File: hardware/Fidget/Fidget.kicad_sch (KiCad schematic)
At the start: 38 parts

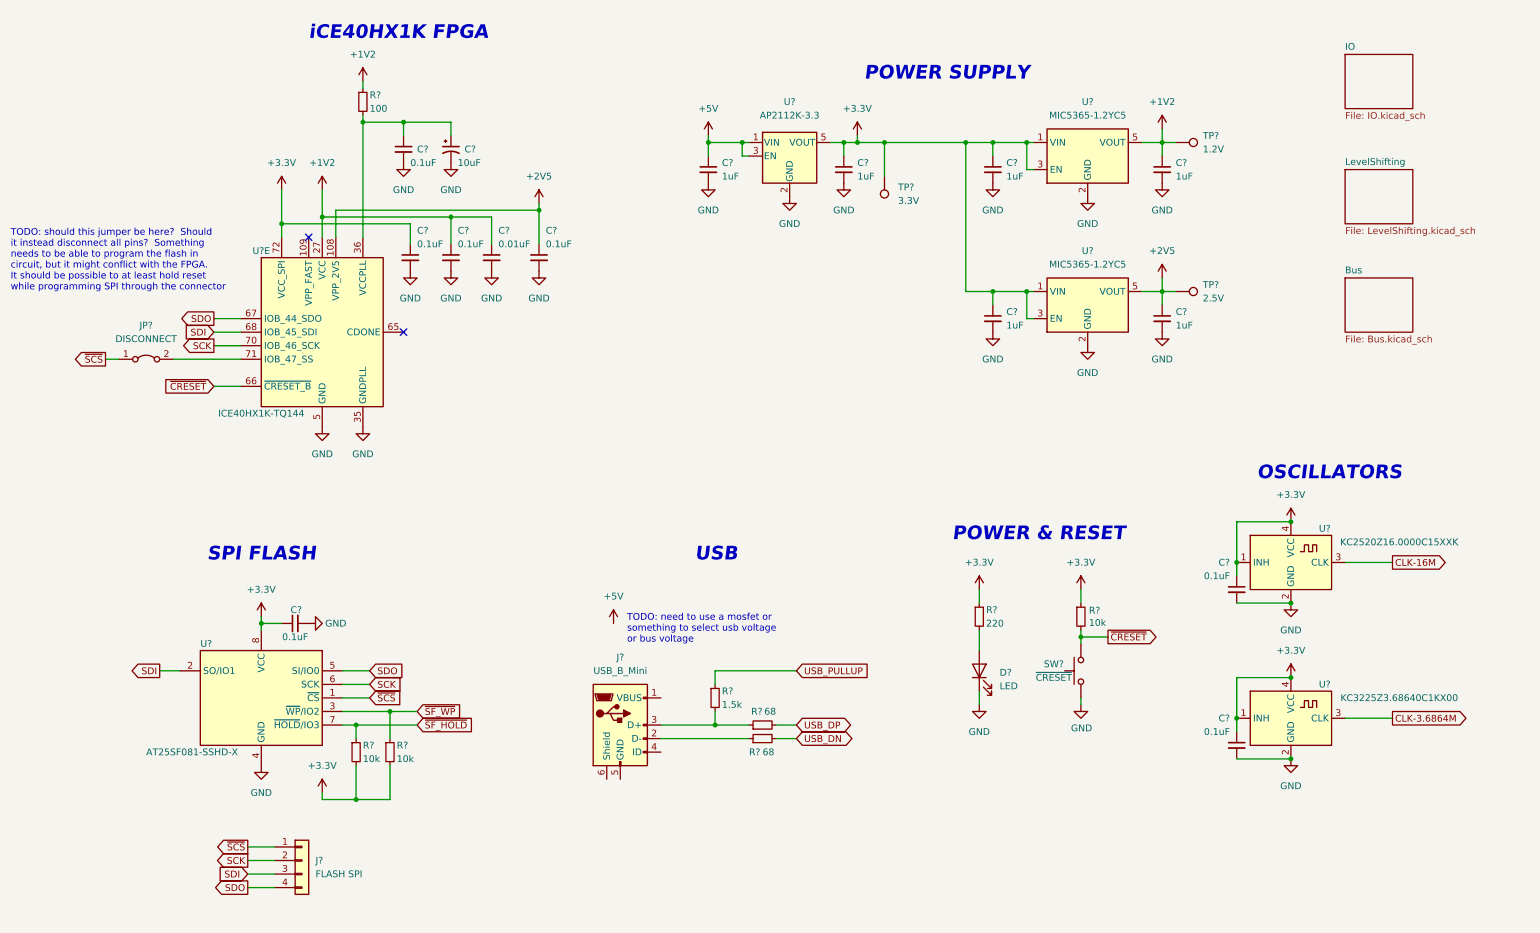
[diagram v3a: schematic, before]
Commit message: Added address latches
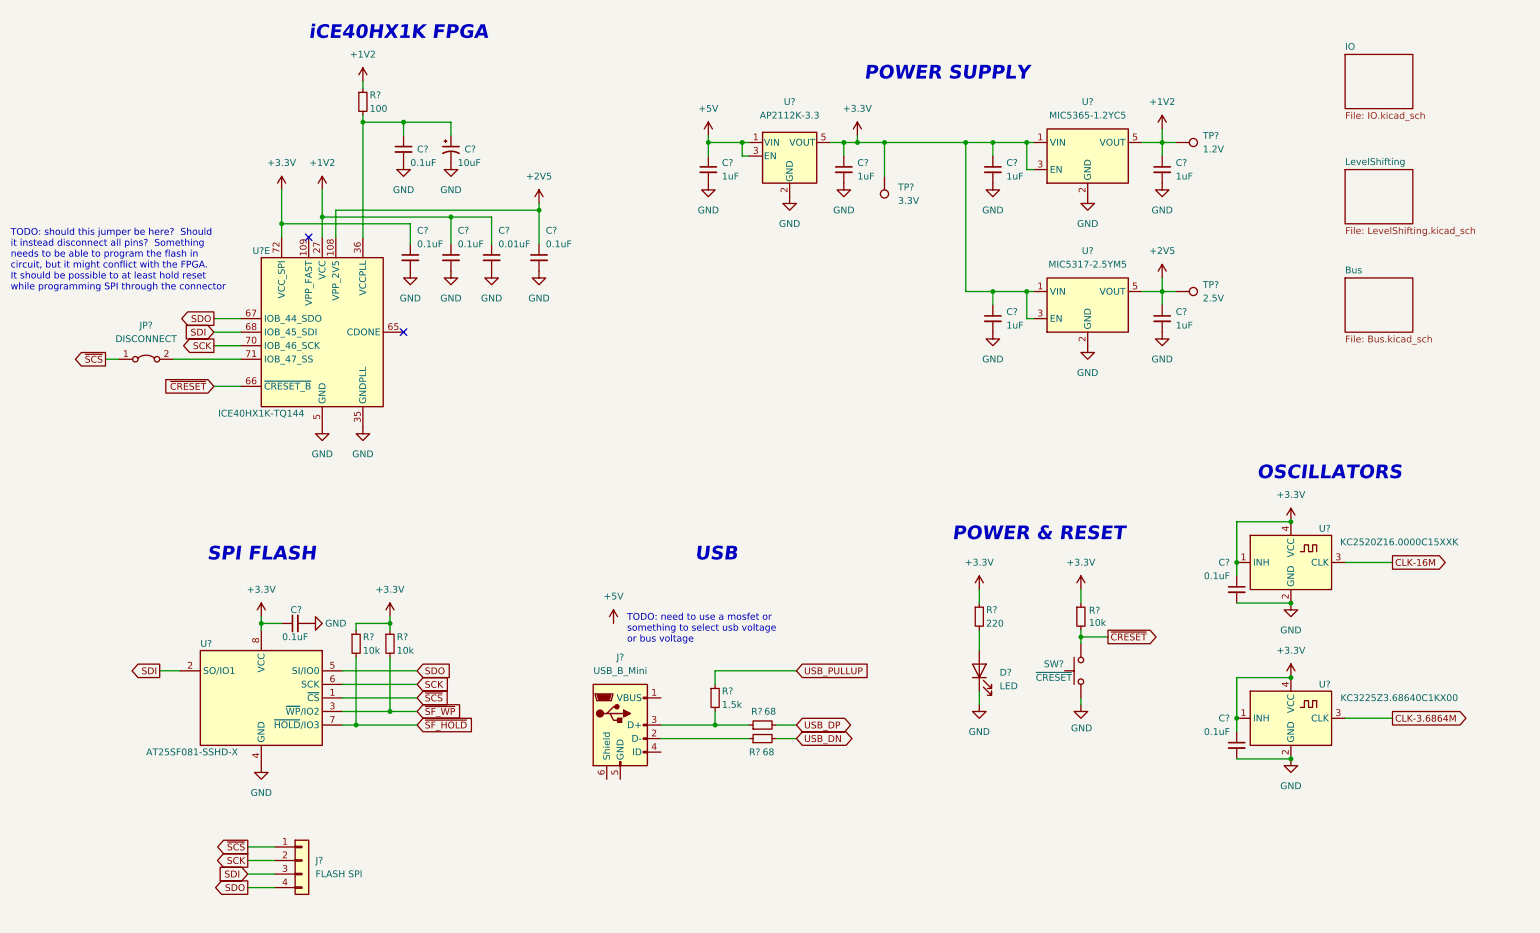
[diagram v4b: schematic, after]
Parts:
- U?: value MIC5365-1.2YC5 -> MIC5317-2.5YM5; footprint Package_TO_SOT_SMD:SOT-353_SC-70-5 -> Package_TO_SOT_SMD:SOT-23-5_HandSoldering
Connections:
- net +3.3V: now also R?.1, R?.1; no longer R?.2, R?.2
- net ~{SF_HOLD}: now also R?.2; no longer R?.1
- net ~{SF_WP}: now also R?.2; no longer R?.1
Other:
- moved on the sheet: R?

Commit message: Added jumper to select bus voltage
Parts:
- added JP?: VBUS, symbol Jumper:Jumper_3_Bridged12
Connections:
- net +3.3V: now also JP?.3 (B)
- net +5V: now also JP?.1 (A)
- new net VBUS: JP?.2 (C)
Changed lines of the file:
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@@
+    (stroke (width 0) (type default) (color 0 0 0 0))
+  )
+  (wire (pts (xy 157.48 71.12) (xy 161.29 71.12))
     (stroke (width 0) (type default) (color 0 0 0 0))
   )
@@
     (stroke (width 0) (type default) (color 0 0 0 0))
   )
+  (wire (pts (xy 140.97 71.12) (xy 144.78 71.12))
+    (stroke (width 0) (type default) (color 0 0 0 0))
+  )
   (wire (pts (xy 196.85 44.45) (xy 195.58 44.45))
     (stroke (width 0) (type default) (color 0 0 0 0))
@@
     (stroke (width 0) (type default) (color 0 0 0 0))
   )
+  (wire (pts (xy 157.48 81.28) (xy 151.13 81.28))
+    (stroke (width 0) (type default) (color 0 0 0 0))
+  )
   (wire (pts (xy 78.74 35.56) (xy 87.63 35.56))
     (stroke (width 0) (type default) (color 0 0 0 0))
@@
     (stroke (width 0) (type default) (color 0 0 0 0))
   )
+  (wire (pts (xy 151.13 81.28) (xy 151.13 74.93))
+    (stroke (width 0) (type default) (color 0 0 0 0))
+  )
   (wire (pts (xy 104.14 52.07) (xy 104.14 58.42))
     (stroke (width 0) (type default) (color 0 0 0 0))
@@
   )
   (wire (pts (xy 55.88 54.61) (xy 80.01 54.61))
+    (stroke (width 0) (type default) (color 0 0 0 0))
+  )
+  (wire (pts (xy 140.97 69.85) (xy 140.97 71.12))
     (stroke (width 0) (type default) (color 0 0 0 0))
   )
@@
     (pin "1")
   )
+  (symbol (lib_id "power:+5V") (at 140.97 69.85 0) (unit 1)
+    (in_bom yes) (on_board yes) (fields_autoplaced)
+    (property "Reference" "#PWR?" (id 0) (at 140.97 73.66 0)
+      (effects (font (size 1.27 1.27)) hide)
+    )
+    (property "Value" "+5V" (id 1) (at 140.97 64.77 0))
+    (property "Footprint" "" (id 2) (at 140.97 69.85 0)
+      (effects (font (size 1.27 1.27)) hide)
+    )
+    (property "Datasheet" "" (id 3) (at 140.97 69.85 0)
+      (effects (font (size 1.27 1.27)) hide)
+    )
+    (pin "1")
+  )
   (symbol (lib_id "power:+3.3V") (at 205.74 123.19 0) (unit 1)
     (in_bom yes) (on_board yes) (fields_autoplaced)
@@
     (pin "8")
   )
+  (symbol (lib_id "power:+3.3V") (at 161.29 71.12 0) (unit 1)
+    (in_bom yes) (on_board yes) (fields_autoplaced)
+    (property "Reference" "#PWR?" (id 0) (at 161.29 74.93 0)
+      (effects (font (size 1.27 1.27)) hide)
+    )
+    (property "Value" "+3.3V" (id 1) (at 161.29 66.04 0))
+    (property "Footprint" "" (id 2) (at 161.29 71.12 0)
+      (effects (font (size 1.27 1.27)) hide)
+    )
+    (property "Datasheet" "" (id 3) (at 161.29 71.12 0)
+      (effects (font (size 1.27 1.27)) hide)
+    )
+    (pin "1")
+  )
+  (symbol (lib_id "power:VBUS") (at 157.48 81.28 0) (unit 1)
+    (in_bom yes) (on_board yes) (fields_autoplaced)
+    (property "Reference" "#PWR?" (id 0) (at 157.48 85.09 0)
+      (effects (font (size 1.27 1.27)) hide)
+    )
+    (property "Value" "VBUS" (id 1) (at 157.48 76.2 0))
+    (property "Footprint" "" (id 2) (at 157.48 81.28 0)
+      (effects (font (size 1.27 1.27)) hide)
+    )
+    (property "Datasheet" "" (id 3) (at 157.48 81.28 0)
+      (effects (font (size 1.27 1.27)) hide)
+    )
+    (pin "1")
+  )
   (symbol (lib_id "Device:R_Small") (at 146.05 148.59 90) (unit 1)
     (in_bom yes) (on_board yes)
@@
     )
     (pin "1")
+  )
+  (symbol (lib_id "Jumper:Jumper_3_Bridged12") (at 151.13 71.12 0) (unit 1)
+    (in_bom yes) (on_board yes) (fields_autoplaced)
+    (property "Reference" "JP?" (id 0) (at 151.13 64.77 0))
+    (property "Value" "VBUS" (id 1) (at 151.13 67.31 0))
+    (property "Footprint" "" (id 2) (at 151.13 71.12 0)
+      (effects (font (size 1.27 1.27)) hide)
+    )
+    (property "Datasheet" "~" (id 3) (at 151.13 71.12 0)
+      (effects (font (size 1.27 1.27)) hide)
+    )
+    (pin "1")
+    (pin "2")
+    (pin "3")
   )
   (symbol (lib_id "power:GND") (at 207.01 77.47 0) (unit 1)
@@
       (reference "#PWR0135") (unit 1) (value "+3.3V") (footprint "")
     )
-    (path "/636ee855-2082-46e2-a822-b2da99283a14/6fc735af-e2e1-4ebe-9b58-edde6986a065"
-      (reference "#PWR0136") (unit 1) (value "+5V") (footprint "")
-    )
     (path "/636ee855-2082-46e2-a822-b2da99283a14/ce525dd6-668d-4227-a847-a3e1bacd0f50"
       (reference "#PWR0137") (unit 1) (value "GND") (footprint "")
@@
       (reference "#PWR?") (unit 1) (value "GND") (footprint "")
     )
+    (path "/636ee855-2082-46e2-a822-b2da99283a14/0c5bded0-c97a-4fbd-beaf-a61fa33b10ae"
+      (reference "#PWR?") (unit 1) (value "VBUS") (footprint "")
+    )
+    (path "/636ee855-2082-46e2-a822-b2da99283a14/0cf0cba3-5d9e-44c7-a28f-17652c4b4436"
+      (reference "#PWR?") (unit 1) (value "VBUS") (footprint "")
+    )
+    (path "/636ee855-2082-46e2-a822-b2da99283a14/10b1bab0-c952-444c-8358-2913aeb4fe24"
+      (reference "#PWR?") (unit 1) (value "VBUS") (footprint "")
+    )
     (path "/636ee855-2082-46e2-a822-b2da99283a14/11563f15-8da5-437f-b4e1-2d5ae629ea03"
       (reference "#PWR?") (unit 1) (value "GND") (footprint "")
@@
       (reference "#PWR?") (unit 1) (value "GND") (footprint "")
     )
-    (path "/f7dd7bf3-1de8-4cd8-8394-417b8f446de5/16f768e4-4e3a-4448-a105-66ad3c56c7a7"
-      (reference "#PWR?") (unit 1) (value "+5V") (footprint "")
-    )
     (path "/f7dd7bf3-1de8-4cd8-8394-417b8f446de5/1d36a57b-949f-4615-b91a-64bfc14f44ee"
       (reference "#PWR?") (unit 1) (value "+5V") (footprint "")
@@
       (reference "#PWR?") (unit 1) (value "+3.3V") (footprint "")
     )
-    (path "/636ee855-2082-46e2-a822-b2da99283a14/2a8c3f81-75f1-4d15-b07e-1c9f0a115830"
-      (reference "#PWR?") (unit 1) (value "+5V") (footprint "")
-    )
     (path "/636ee855-2082-46e2-a822-b2da99283a14/2fe51a8a-67b4-4a30-813c-964e08046c9a"
       (reference "#PWR?") (unit 1) (value "+3.3V") (footprint "")
@@
       (reference "#PWR?") (unit 1) (value "GND") (footprint "")
     )
-    (path "/636ee855-2082-46e2-a822-b2da99283a14/3fd2297e-5698-4642-bc2d-58f967eed514"
-      (reference "#PWR?") (unit 1) (value "+5V") (footprint "")
-    )
     (path "/636ee855-2082-46e2-a822-b2da99283a14/41551522-02c1-4dd1-9a34-797ac50d4a62"
       (reference "#PWR?") (unit 1) (value "GND") (footprint "")
@@
       (reference "#PWR?") (unit 1) (value "+3.3V") (footprint "")
     )
+    (path "/f7dd7bf3-1de8-4cd8-8394-417b8f446de5/4c6a86c6-8e70-455e-b0f1-3a85d9c38783"
+      (reference "#PWR?") (unit 1) (value "VBUS") (footprint "")
+    )
     (path "/f7dd7bf3-1de8-4cd8-8394-417b8f446de5/5180021b-7a96-41d6-9914-21063da06687"
       (reference "#PWR?") (unit 1) (value "+5V") (footprint "")
@@
       (reference "#PWR?") (unit 1) (value "GND") (footprint "")
     )
+    (path "/636ee855-2082-46e2-a822-b2da99283a14/59127b2b-6701-4a2b-9259-206188fd9e7b"
+      (reference "#PWR?") (unit 1) (value "VBUS") (footprint "")
+    )
     (path "/636ee855-2082-46e2-a822-b2da99283a14/5c47910f-4b06-4a60-84b7-8b839591c7b0"
       (reference "#PWR?") (unit 1) (value "GND") (footprint "")
@@
       (reference "#PWR?") (unit 1) (value "+3.3V") (footprint "")
     )
-    (path "/636ee855-2082-46e2-a822-b2da99283a14/69955695-b4d6-4fa5-bee2-36776a1e7f05"
-      (reference "#PWR?") (unit 1) (value "+5V") (footprint "")
-    )
     (path "/74a457dd-b247-4fca-ac95-a20e3550b50d"
       (reference "#PWR?") (unit 1) (value "+3.3V") (footprint "")
@@
       (reference "#PWR?") (unit 1) (value "GND") (footprint "")
     )
+    (path "/7ceff54d-8f64-40e0-bd7e-3898de1dd818"
+      (reference "#PWR?") (unit 1) (value "+5V") (footprint "")
+    )
     (path "/f7dd7bf3-1de8-4cd8-8394-417b8f446de5/7fed7f87-57f9-4557-b78f-a90ebde90d03"
       (reference "#PWR?") (unit 1) (value "GND") (footprint "")
@@
       (reference "#PWR?") (unit 1) (value "GND") (footprint "")
     )
-    (path "/636ee855-2082-46e2-a822-b2da99283a14/abe0ae81-f672-420f-91b1-89e8ab7bd21d"
-      (reference "#PWR?") (unit 1) (value "+5V") (footprint "")
+    (path "/636ee855-2082-46e2-a822-b2da99283a14/a6e5f6f8-4983-430c-8700-72d42084968b"
+      (reference "#PWR?") (unit 1) (value "VBUS") (footprint "")
+    )
+    (path "/a78020b8-687c-4be9-911e-e0cd2086d5d8"
+      (reference "#PWR?") (unit 1) (value "+3.3V") (footprint "")
+    )
+    (path "/a82892fa-c929-4808-97fc-d11a0d96ce15"
+      (reference "#PWR?") (unit 1) (value "VBUS") (footprint "")
     )
     (path "/b24e0aa7-2b07-48ac-950b-0efc27378c2d"
@@
       (reference "#PWR?") (unit 1) (value "GND") (footprint "")
     )
-    (path "/636ee855-2082-46e2-a822-b2da99283a14/c51a05ba-583d-4bf0-bd18-07a49d5ea6d4"
-      (reference "#PWR?") (unit 1) (value "+5V") (footprint "")
-    )
     (path "/636ee855-2082-46e2-a822-b2da99283a14/c8cdb7fc-9fec-48d3-a99a-1b967e98e7d0"
       (reference "#PWR?") (unit 1) (value "GND") (footprint "")
@@
       (reference "#PWR?") (unit 1) (value "GND") (footprint "")
     )
+    (path "/636ee855-2082-46e2-a822-b2da99283a14/df9b1ef6-456a-4cfe-afb2-64e70499168b"
+      (reference "#PWR?") (unit 1) (value "VBUS") (footprint "")
+    )
     (path "/e373c404-3471-489f-9afd-666153137375"
       (reference "#PWR?") (unit 1) (value "GND") (footprint "")
@@
       (reference "JP?") (unit 1) (value "DISCONNECT") (footprint "")
     )
+    (path "/b35cdbc6-920f-4341-879b-9c4d75f4de0a"
+      (reference "JP?") (unit 1) (value "VBUS") (footprint "")
+    )
     (path "/005daac8-fd10-4827-b91b-63226d46d5c5"

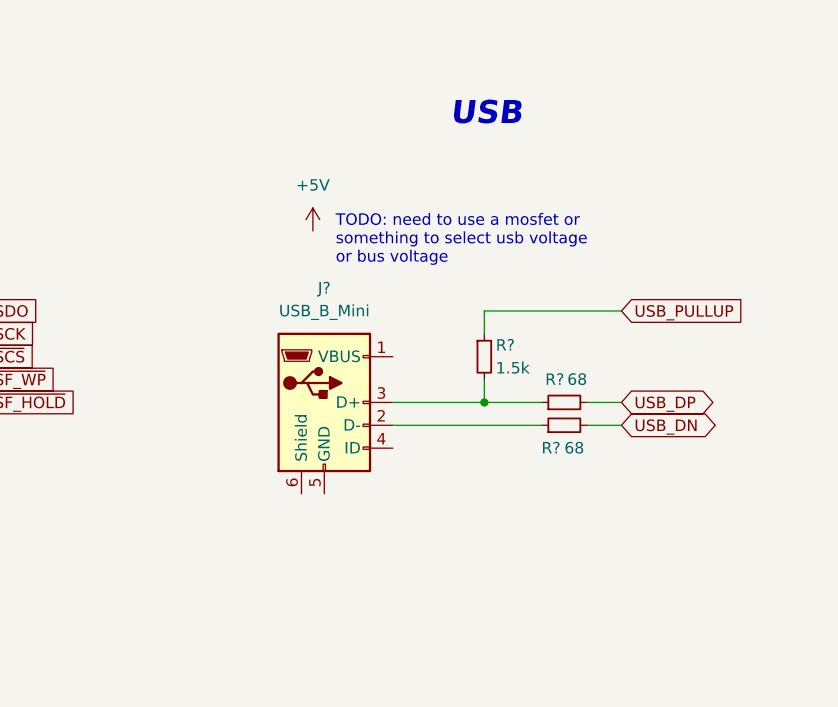
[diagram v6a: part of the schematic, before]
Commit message: Filled in more details in schematic
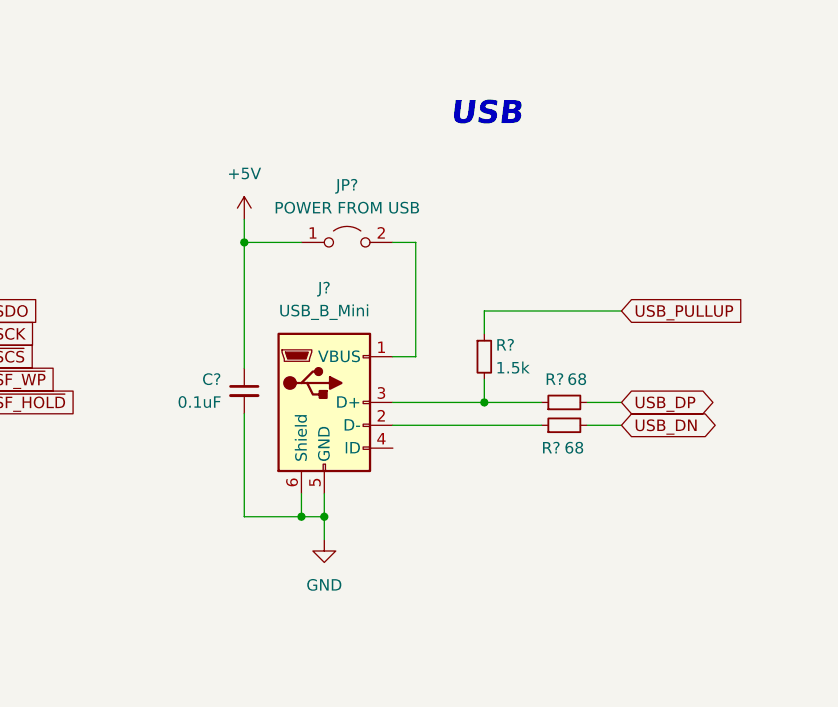
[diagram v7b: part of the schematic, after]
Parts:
- added C?: 0.1uF, symbol Device:C_Small
- added JP?: POWER FROM USB, symbol Jumper:Jumper_2_Open
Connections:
- net +5V: now also C?.1, JP?.1 (A)
- net GND: now also J?.5 (GND), J?.6 (Shield), C?.2
- net at J?.1 (VBUS): now also JP?.2 (B)
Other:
- note removed: "TODO: need to use a mosfet or something to select usb voltage or bus voltage"
